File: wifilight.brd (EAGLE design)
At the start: 48.3 x 48.3 mm, 37 parts, among them Q1 BUK98180-100A, Q2 BUK98180-100A, Q3 BUK98180-100A, Q4 BUK98180-100A, U1 TCA6507PW, X1 53261-06

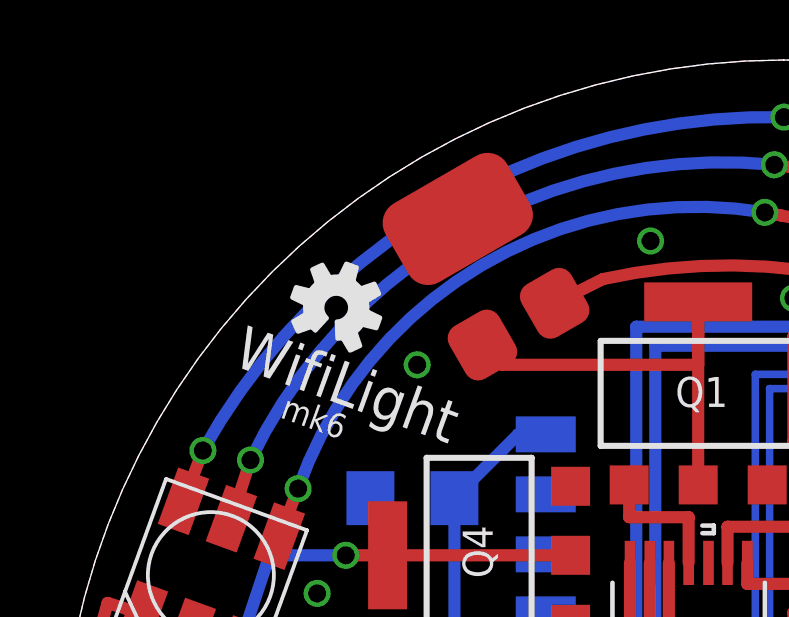
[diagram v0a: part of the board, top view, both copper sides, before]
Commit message: Made mofications to schematics for readability
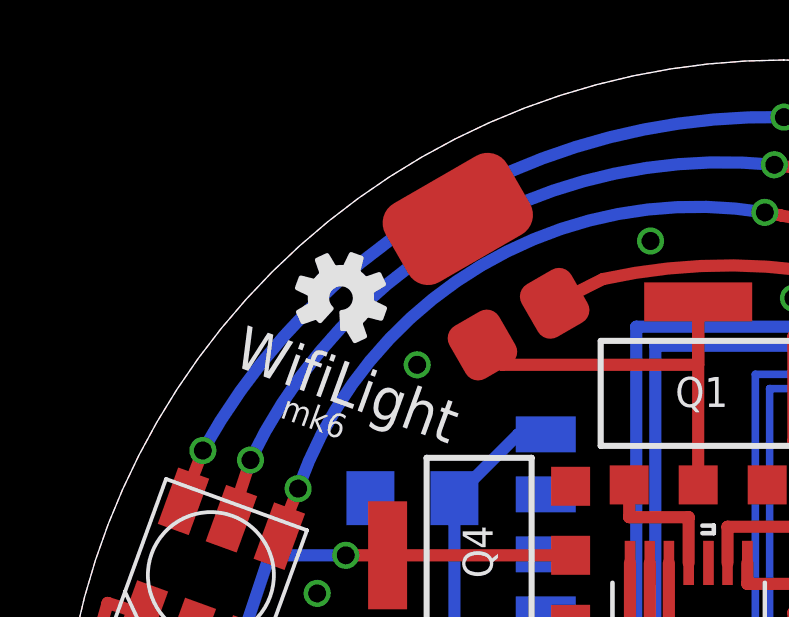
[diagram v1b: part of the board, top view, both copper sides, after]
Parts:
- removed U$2: (no value), SparkFun-Aesthetics:OSHW-LOGO-S
- added FRAME1: (no value), SparkFun-Aesthetics:DUMMY
- added LOGO1: OSHW-LOGOS, SparkFun-Aesthetics:OSHW-LOGO-S
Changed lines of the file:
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@@
 <attribute name="NAME" x="40.79875" y="35.21075" size="0.8128" layer="26" rot="MR180"/>
 </element>
-<element name="U$2" library="SparkFun-Aesthetics" package="OSHW-LOGO-S" value="" x="10.4775" y="41.275" rot="R340"/>
+<element name="LOGO1" library="SparkFun-Aesthetics" package="OSHW-LOGO-S" value="OSHW-LOGOS" x="10.63625" y="41.5925" rot="R340"/>
+<element name="FRAME1" library="SparkFun-Aesthetics" package="DUMMY" value="" x="2.2225" y="-2.8575">
+<attribute name="VERSION" value="v01" x="1.27" y="-1.74625" size="1.778" layer="27" display="off"/>
+<attribute name="DESIGNER" value="Nobody" x="1.27" y="-1.74625" size="1.778" layer="27" display="off"/>
+</element>
 </elements>
 <signals>
@@
 <via x="13.17625" y="39.37" extent="1-16" drill="0.6"/>
 <via x="20.955" y="43.4975" extent="1-16" drill="0.6"/>
-<wire x1="25.7175" y1="41.5925" x2="20.955" y2="43.4975" width="0" layer="19" extent="1-1"/>
 </signal>
 <signal name="SCL">

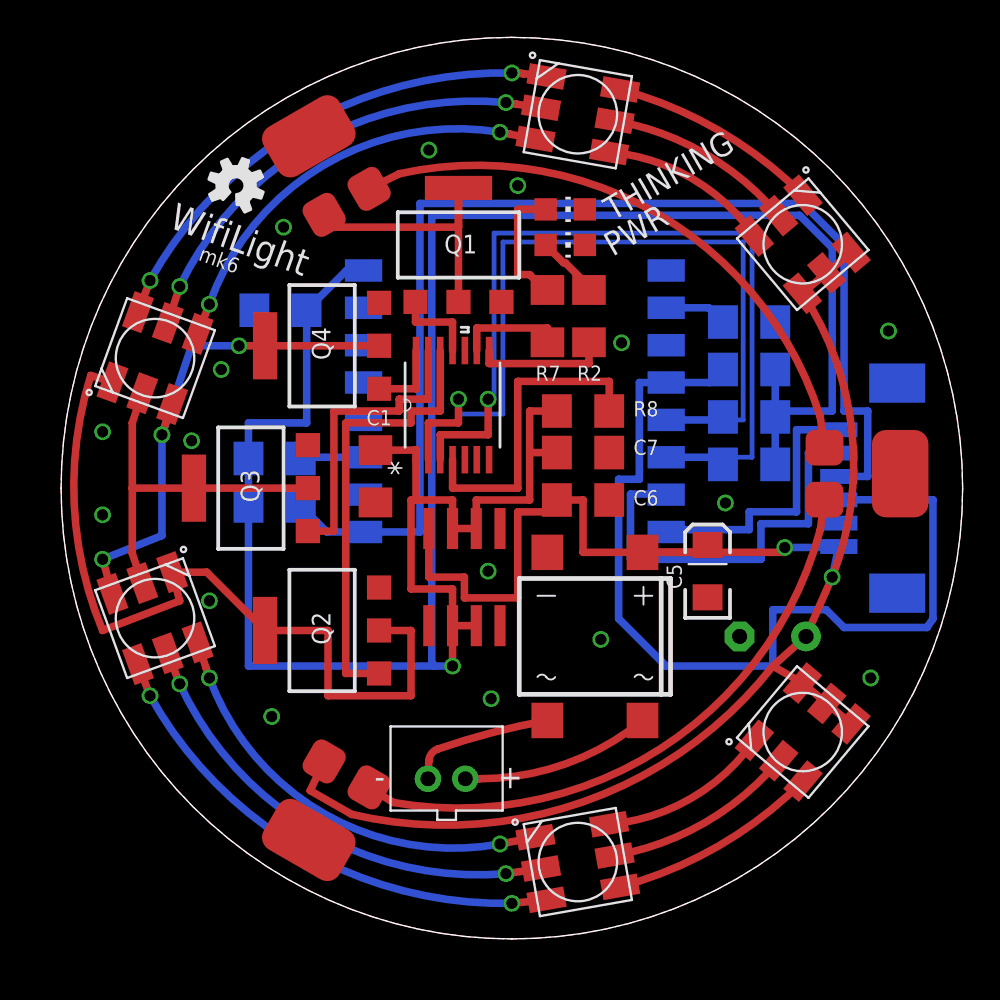
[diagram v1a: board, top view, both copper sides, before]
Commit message: Revised to use larger regulators, Revised to use 4 layers
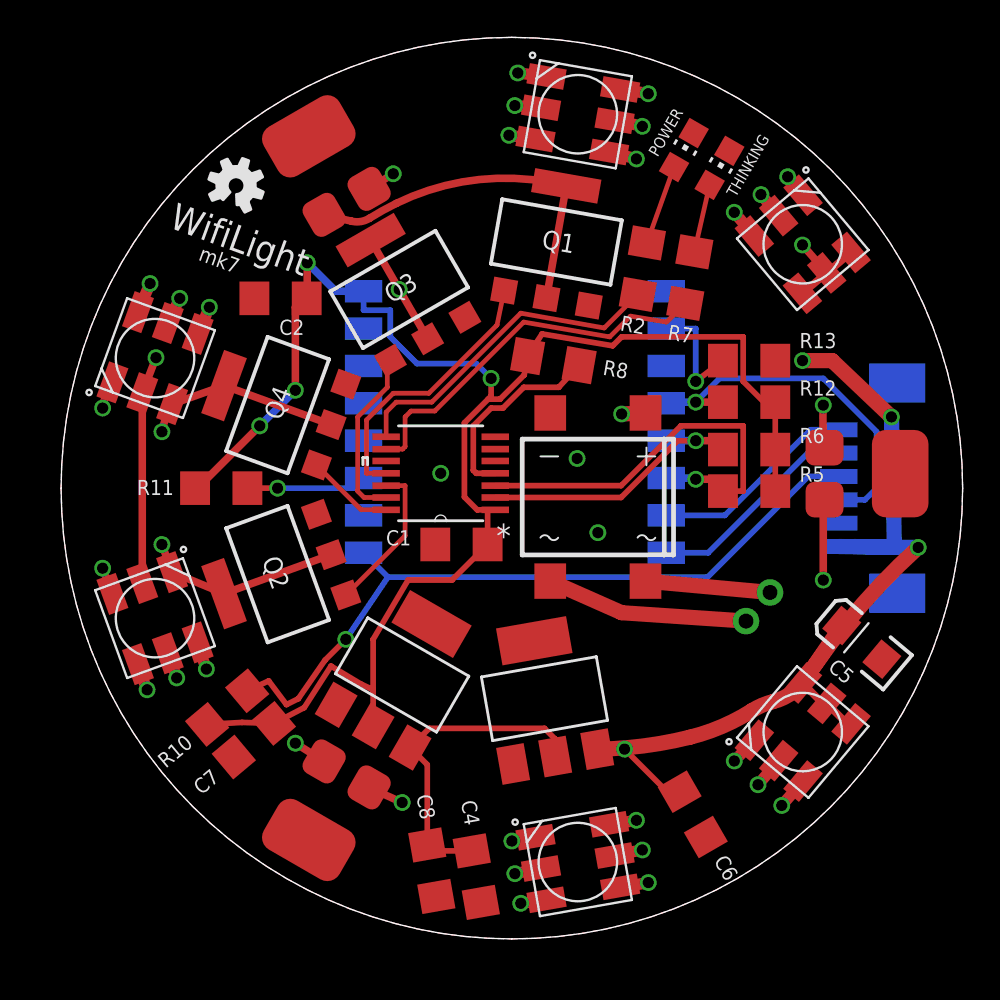
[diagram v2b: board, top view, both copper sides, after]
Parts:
- removed C3: (no value), rcl:E3,5-8
- removed PWR: (no value), led:CHIP-LED0805
- removed REG2: MC33269-SO8, linear:SO08
- added C4: 0.1uF, SparkFun-Passives:1206
- added C8: 10uF, SparkFun-Passives:1206
- added IC1, IC2: REG1117, burr-brown:SOT223
- added POWER: (no value), led:CHIP-LED0805
- moved C7 23.4 mm to (11.6, 11.9), turned to 220 degrees
- moved CN1 19.0 mm to (38.6, 19.1), flipped to the bottom, turned to 130 degrees
- moved C6 17.8 mm to (35.1, 7.94), turned to 300 degrees
- moved Q3 13.3 mm to (19.4, 36.0), turned to 30 degrees
- moved R10 11.1 mm to (10.2, 13.7), flipped to the top, turned to 40 degrees
- moved C5 9.09 mm to (44.1, 17.1), turned to 140 degrees
- moved THINKING 8.55 mm to (36.5, 42.5), turned to 330 degrees
- moved R7 7.89 mm to (34.9, 36.7), turned to 80 degrees
- moved B2 7.46 mm to (30.0, 24.9)
- moved C1 5.88 mm to (22.7, 22.4), turned to 180 degrees
- moved Q1 5.24 mm to (27.8, 38.6), turned to 350 degrees
- moved Q4 3.97 mm to (12.9, 29.8), turned to 70 degrees
- moved Q2 3.84 mm to (12.9, 20.8), turned to 110 degrees
- moved R2 3.82 mm to (32.4, 37.1), turned to 80 degrees
- moved U1 3.71 mm to (21.6, 26.2), turned to 180 degrees
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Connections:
- new net 5V: C4.1, C8.1, IC1.2, IC2.3
- net 12V: now also IC1.3; no longer C3.+, REG2.4
- net 3.3V: now also IC2.2; no longer REG2.2, REG2.3, REG2.6, REG2.7
- net GND: now also C4.2, C8.2, IC1.1, IC2.1, POWER.C; no longer C3.-, PWR.C, REG2.1
- net N$14: now also POWER.A; no longer PWR.A
- net RXD: now also X1.1; no longer X1.2
- net TXD: now also X1.2; no longer X1.1
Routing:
- net 3.3V: track 134.5 -> 88.9 mm, vias 1 -> 4
- net GPIO0: track 51.5 -> 19.8 mm, vias 0 -> 1
- net SCL: track 46.8 -> 15.4 mm
- net SDA: track 48.6 -> 22.9 mm
- net RESET: track 63.4 -> 39.9 mm, vias 0 -> 1
- net P_BLUE: track 43.7 -> 20.2 mm, vias 0 -> 2
- net 5V: track 0.00 -> 17.5 mm
- net BLUE: track 24.1 -> 8.19 mm
- net THINKING: track 5.76 -> 20.7 mm
- net P_RED: track 19.7 -> 31.9 mm, vias 0 -> 2
- net RXD: track 22.3 -> 11.1 mm
- net POWERED: track 7.19 -> 17.8 mm
- net WHITE: track 4.58 -> 14.9 mm
- net 12V: track 97.3 -> 106.0 mm, vias 2 -> 7
- net P_GREEN: track 27.5 -> 20.1 mm, vias 3 -> 2
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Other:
- board text added: "mk7"
- board text removed: "mk6"

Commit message: Mk8 gets its PCA9685 back, the older LED controller turned out to only have 2 channels of PWM available, which is insufficient. Respan this board with 3xRGB 5050's and 3xLuxeon rebels. reduced complexity lets us have 2 layer boards again. Almost everything 'cept the MCU is on the front, save for 4 resistors and the programming harness. May still have to flip RX & TX
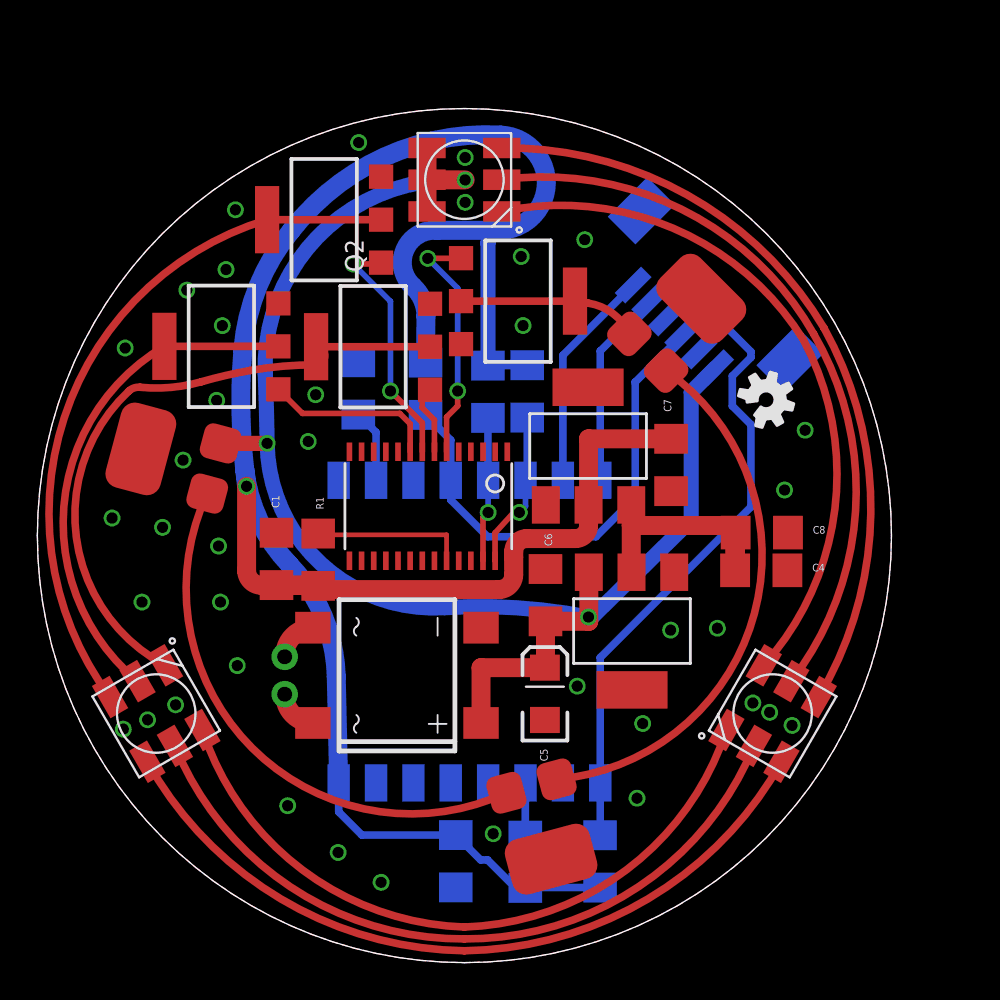
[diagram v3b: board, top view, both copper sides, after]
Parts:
- removed FRAME1: (no value), SparkFun-Aesthetics:DUMMY
- removed LED4, LED5, LED6: RGBLED5050, adafruit:RGBLED5050
- removed POWER, THINKING: (no value), led:CHIP-LED0805
- removed R2, R7: 220ohm, SparkFun-Passives:1206
- removed R8: 10K, SparkFun-Passives:1206
- added R1: (no value), SparkFun-Resistors:1206
- U1: value TCA6507PW -> (none); device Texas Instruments_By_element14_Batch_1:SOP65P640X120-14N -> adafruit:TSSOP28
- moved LED1 34.7 mm to (22.9, 41.9), turned to 0 degrees
- moved C2 31.6 mm to (22.4, 5.43), flipped to the bottom, turned to 270 degrees
- moved LOGO1 30.6 mm to (39.0, 30.1), turned to 300 degrees
- moved MPU 28.5 mm to (14.1, 9.62), turned to 90 degrees
- moved C7 26.8 mm to (33.9, 26.6), turned to 270 degrees
- moved WL2 26.1 mm to (27.1, 6.91), turned to 15 degrees
- moved R11 25.8 mm to (26.1, 5.40), flipped to the bottom, turned to 90 degrees
- moved CN1 25.6 mm to (13.2, 15.4), turned to 270 degrees
- moved C8 25.3 mm to (38.8, 23.0), turned to 0 degrees
- moved C4 22.4 mm to (38.8, 21.0), turned to 0 degrees
- moved R10 21.6 mm to (30.1, 5.42), flipped to the bottom, turned to 90 degrees
- moved WL1 21.1 mm to (34.5, 34.5), turned to 135 degrees
- moved WL3 21.1 mm to (6.91, 27.1), turned to 255 degrees
- moved R13 21.0 mm to (17.2, 30.7), flipped to the bottom, turned to 270 degrees
- moved R12 17.3 mm to (20.8, 30.7), flipped to the bottom, turned to 270 degrees
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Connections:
- removed net EN: R8.2, U1.4
- removed net N$14: POWER.A, R2.2
- removed net N$15: R7.2, THINKING.A
- removed net N$37: LED4.5, LED5.2
- removed net N$38: LED4.6, LED5.1
- removed net N$39: LED4.4, LED5.3
- removed net N$40: LED5.5, LED6.2
- removed net N$41: LED5.6, LED6.1
- removed net N$42: LED5.4, LED6.3
- removed net N$6: U1.10
- removed net POWERED: R2.1, U1.8
- removed net THINKING: R7.1, U1.9
- new net #OE: R1.1, U1.23
- net 12V: no longer LED4.1, LED4.2, LED4.3
- net 3.3V: now also R1.2, U1.28; no longer R8.1, U1.1
- net BLUE: now also U1.7; no longer U1.12
- net GND: now also U1.1, U1.14, U1.2, U1.24, U1.25, U1.3, U1.4; no longer POWER.C, THINKING.C, U1.6, U1.7
- net GREEN: now also U1.8; no longer U1.14
- net P_BLUE: no longer LED6.4
- net P_GREEN: no longer LED6.6
- net P_RED: no longer LED6.5
- net RED: now also U1.9; no longer U1.13
- net SCL: now also U1.26; no longer U1.2
- net SDA: now also U1.27; no longer U1.3
- net WHITE: now also U1.6; no longer U1.11
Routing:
- net 3.3V: track 88.9 -> 126.0 mm, vias 4 -> 1
- net N$34: track 11.5 -> 39.5 mm, vias 2 -> 0
- net N$33: track 10.3 -> 37.3 mm, vias 2 -> 0
- net N$35: track 9.15 -> 35.1 mm, vias 2 -> 0
- net N$42: track 25.9 -> 0.00 mm, vias 2 -> 0
- net 12V: track 106.0 -> 80.2 mm, vias 7 -> 3
- net N$40: track 23.6 -> 0.00 mm, vias 2 -> 0
- net N$41: track 21.5 -> 0.00 mm, vias 2 -> 0
- net THINKING: track 20.7 -> 0.00 mm
- net POWERED: track 17.8 -> 0.00 mm
- net SDA: track 22.9 -> 8.58 mm
- net N$31: track 25.9 -> 39.5 mm, vias 2 -> 0
- net N$32: track 21.5 -> 35.1 mm, vias 2 -> 0
- net N$30: track 23.7 -> 37.3 mm, vias 2 -> 0
- net P_GREEN: track 20.1 -> 33.0 mm, vias 2 -> 0
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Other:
- board size 48.3 x 48.3 mm -> 45.7 x 45.7 mm
- board text removed: "WifiLight"
- board text removed: "mk7"

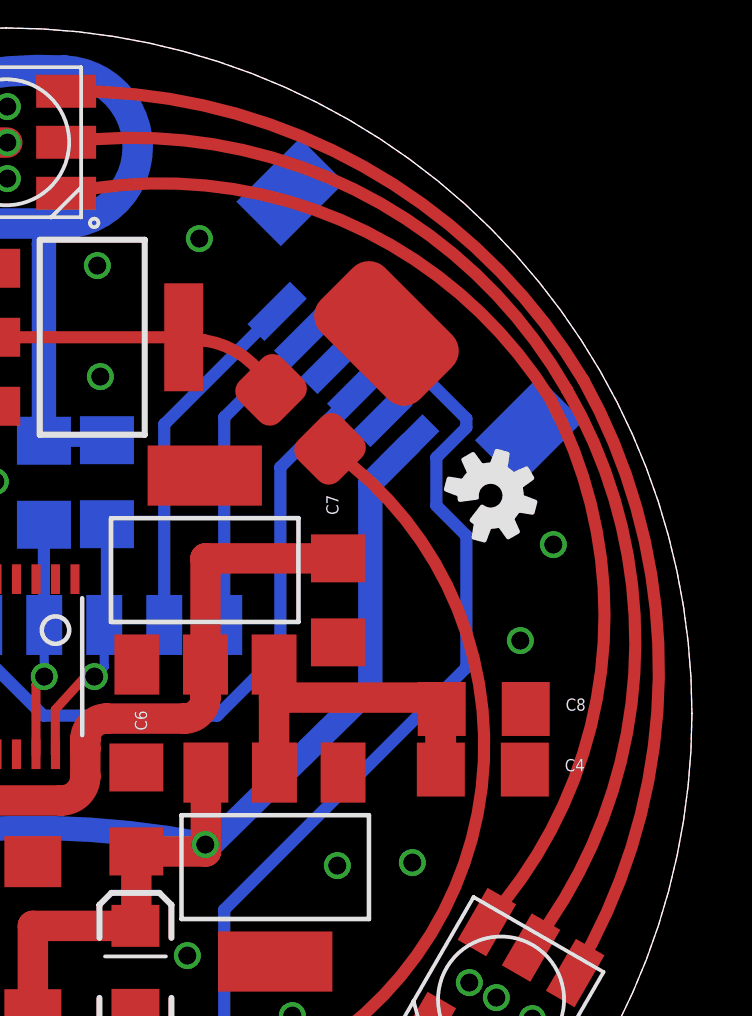
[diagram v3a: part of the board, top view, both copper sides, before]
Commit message: Add ICSP header. Resolves #5
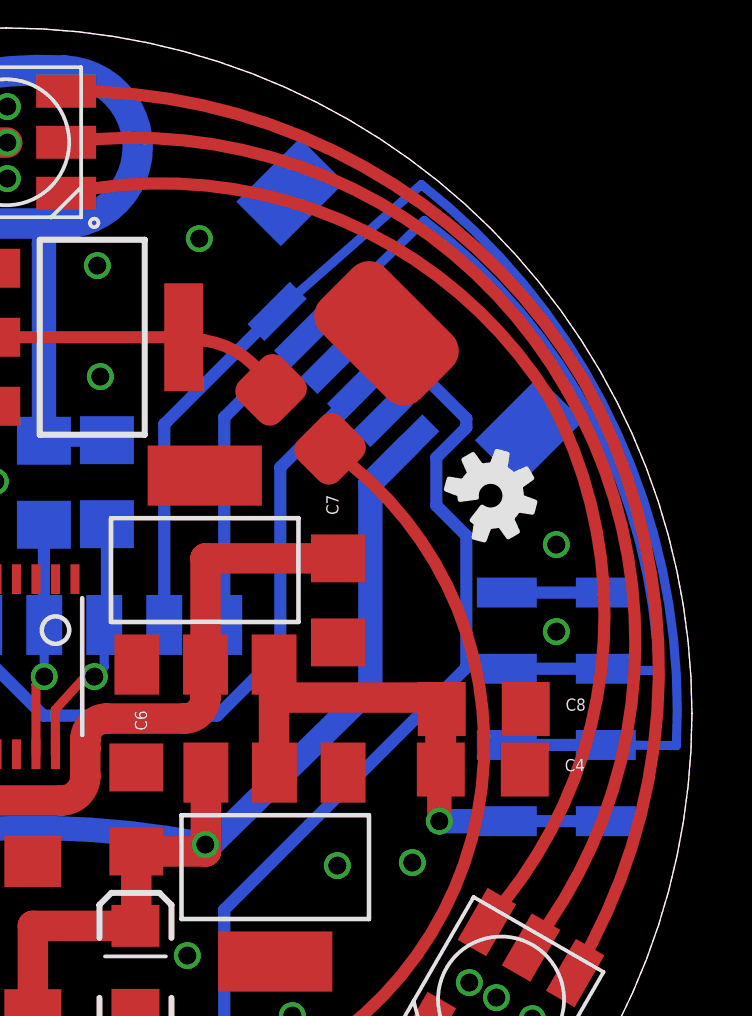
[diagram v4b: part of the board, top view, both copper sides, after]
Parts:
- added ICSP: 1X04_SMD_STRAIGHT_COMBO, SparkFun-Connectors:1X04_SMD_STRAIGHT_COMBO
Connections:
- net 5V: now also ICSP.4
- net GND: now also ICSP.1
- net RXD: now also ICSP.3
- net TXD: now also ICSP.2
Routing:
- net RXD: track 12.0 -> 41.3 mm
- net TXD: track 10.7 -> 39.1 mm
- net 5V: track 13.6 -> 17.6 mm, vias 0 -> 1
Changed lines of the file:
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@@
 <grid distance="0.00393700787" unitdist="inch" unit="inch" style="lines" multiple="1" display="no" altdistance="0.025" altunitdist="inch" altunit="inch"/>
 <layers>
-<layer number="1" name="Top" color="4" fill="1" visible="yes" active="yes"/>
+<layer number="1" name="Top" color="4" fill="1" visible="no" active="yes"/>
 <layer number="2" name="Route2" color="1" fill="3" visible="no" active="no"/>
 <layer number="3" name="Route3" color="4" fill="3" visible="no" active="no"/>
@@
 <attribute name="VALUE" x="37.81454375" y="33.178346875" size="1.27" layer="28" rot="MR45"/>
 </element>
+<element name="ICSP" library="SparkFun-Connectors" package="1X04_SMD_STRAIGHT_COMBO" value="1X04_SMD_STRAIGHT_COMBO" x="41.2" y="26.9" smashed="yes" rot="MR270">
+<attribute name="PROD_ID" value="CONN-08511" x="41.2" y="26.9" size="1.778" layer="28" rot="MR270" display="off"/>
+<attribute name="NAME" x="39.079" y="26.4" size="1.27" layer="26" ratio="10" rot="MR270"/>
+</element>
 </elements>
 <signals>
@@
 <via x="38.3" y="13.9" extent="1-16" drill="0.6"/>
 <via x="36.4" y="17.9" extent="1-16" drill="0.6"/>
-<via x="40" y="25.3" extent="1-16" drill="0.6"/>
-<via x="41.1" y="28.5" extent="1-16" drill="0.6"/>
+<via x="41.2" y="25.6" extent="1-16" drill="0.6"/>
+<via x="41.2" y="28.5" extent="1-16" drill="0.6"/>
+<contactref element="ICSP" pad="1"/>
 </signal>
 <signal name="SCL">
@@
 <contactref element="X1" pad="2"/>
 <wire x1="30.13" y1="25.82" x2="30.13" y2="32.741646875" width="0.4064" layer="16"/>
-<wire x1="30.13" y1="32.741646875" x2="32.776409375" y2="35.38805625" width="0.4064" layer="16"/>
+<wire x1="30.13" y1="32.741646875" x2="32.194178125" y2="34.805825" width="0.4064" layer="16"/>
+<contactref element="ICSP" pad="2"/>
+<wire x1="32.194178125" y1="34.805825" x2="32.776409375" y2="35.38805625" width="0.4064" layer="16"/>
+<wire x1="39.55" y1="24.36" x2="44.6" y2="24.3" width="0.3048" layer="16"/>
+<wire x1="44.6" y1="24.3" x2="36.8" y2="39.3" width="0.3048" layer="16" curve="51"/>
+<wire x1="36.8" y1="39.3" x2="32.194178125" y2="34.805825" width="0.3048" layer="16"/>
 </signal>
 <signal name="RXD">
@@
 <wire x1="28.13" y1="25.82" x2="28.13" y2="32.509415625" width="0.4064" layer="16"/>
 <wire x1="28.13" y1="32.509415625" x2="31.892525" y2="36.271940625" width="0.4064" layer="16"/>
+<contactref element="ICSP" pad="3"/>
+<wire x1="42.85" y1="21.82" x2="45.2" y2="21.8" width="0.3048" layer="16"/>
+<wire x1="45.2" y1="21.8" x2="36.7" y2="40.5" width="0.3048" layer="16" curve="55"/>
+<wire x1="36.7" y1="40.5" x2="31.892525" y2="36.271940625" width="0.3048" layer="16"/>
 </signal>
 <signal name="GPIO15">
@@
 <wire x1="37.35" y1="21" x2="37.35" y2="23.4" width="1.016" layer="1"/>
 <wire x1="37.35" y1="23.4" x2="31.7914" y2="23.4" width="1.016" layer="1"/>
+<contactref element="ICSP" pad="4"/>
+<wire x1="39.55" y1="19.28" x2="37.3" y2="19.28" width="0.8128" layer="16"/>
+<via x="37.3" y="19.28" extent="1-16" drill="0.6"/>
+<wire x1="37.3" y1="19.28" x2="37.3" y2="21" width="0.8128" layer="1"/>
+<wire x1="37.3" y1="21" x2="37.35" y2="21" width="0.3048" layer="1"/>
 </signal>
 <signal name="#OE">
@@
 </signal>
 </signals>
+<errors>
+</errors>
 </board>
 </drawing>
